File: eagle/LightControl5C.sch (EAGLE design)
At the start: 36 parts, among them IC1 LV3842XF, IC2 PIC12F675, IC3 7805, U1 ULN2003D, X1 Footprint, X10 Footprint, X11 Footprint, X2 Footprint, X3 FLE-103-01, X4 Footprint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

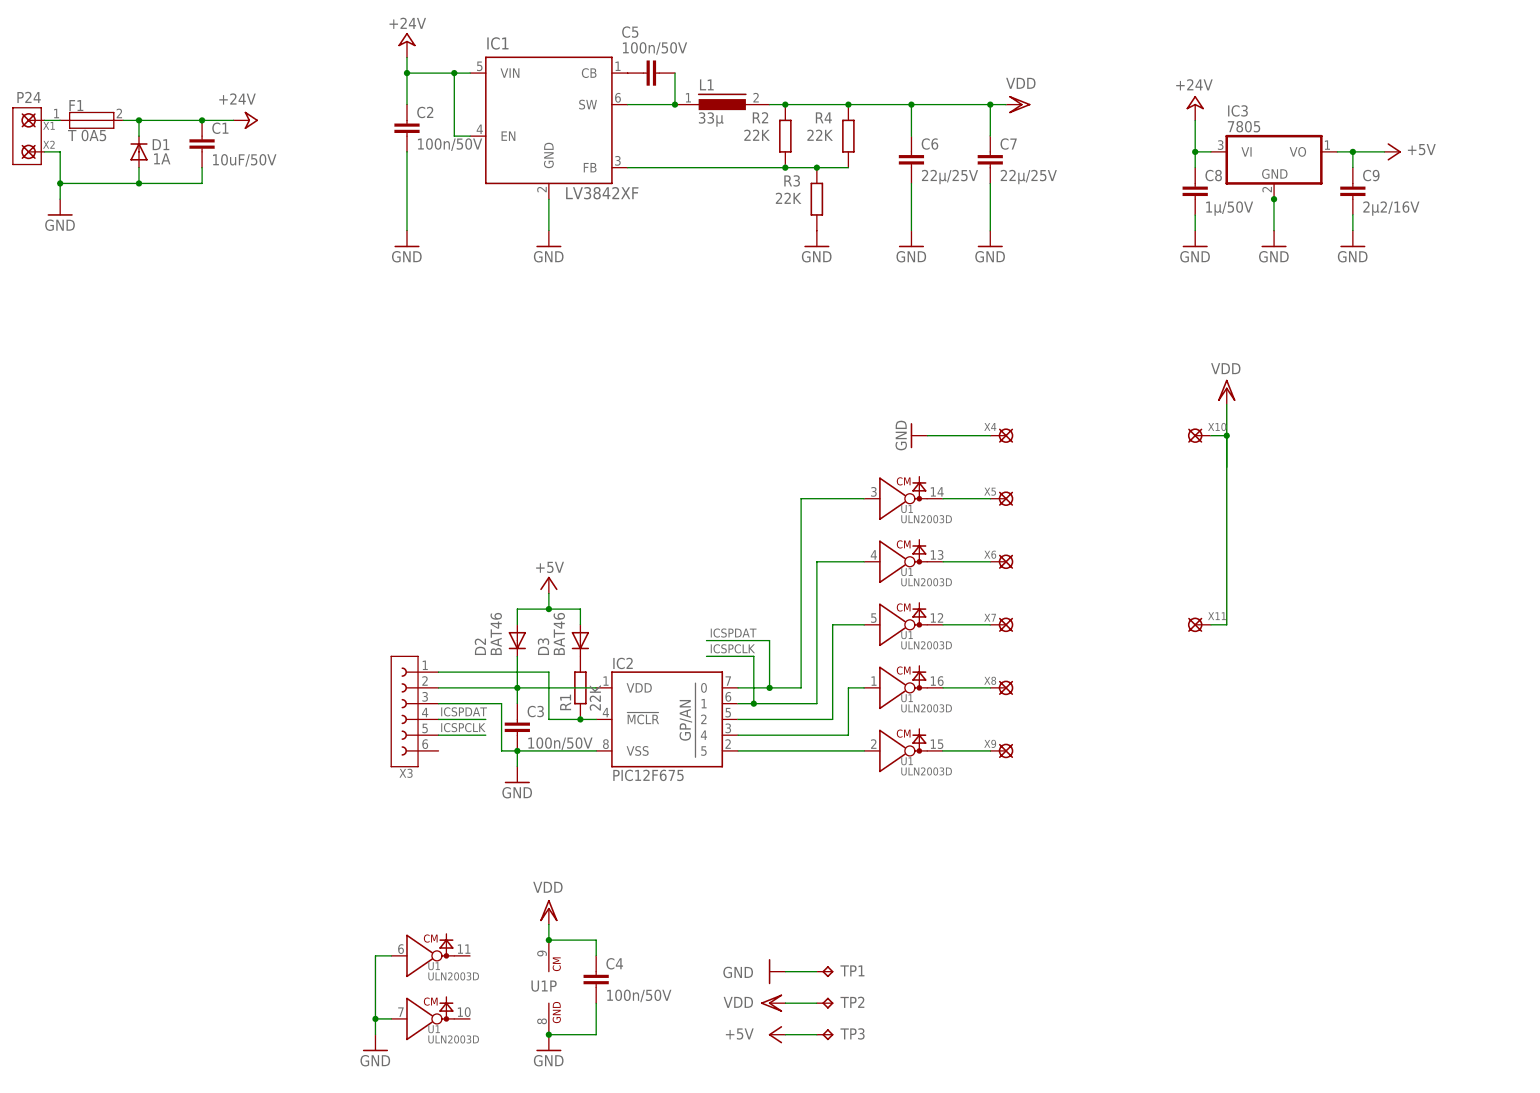
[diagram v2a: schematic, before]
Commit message: [eagle] change inductor
-> increase min. inductor size to allow lower currents
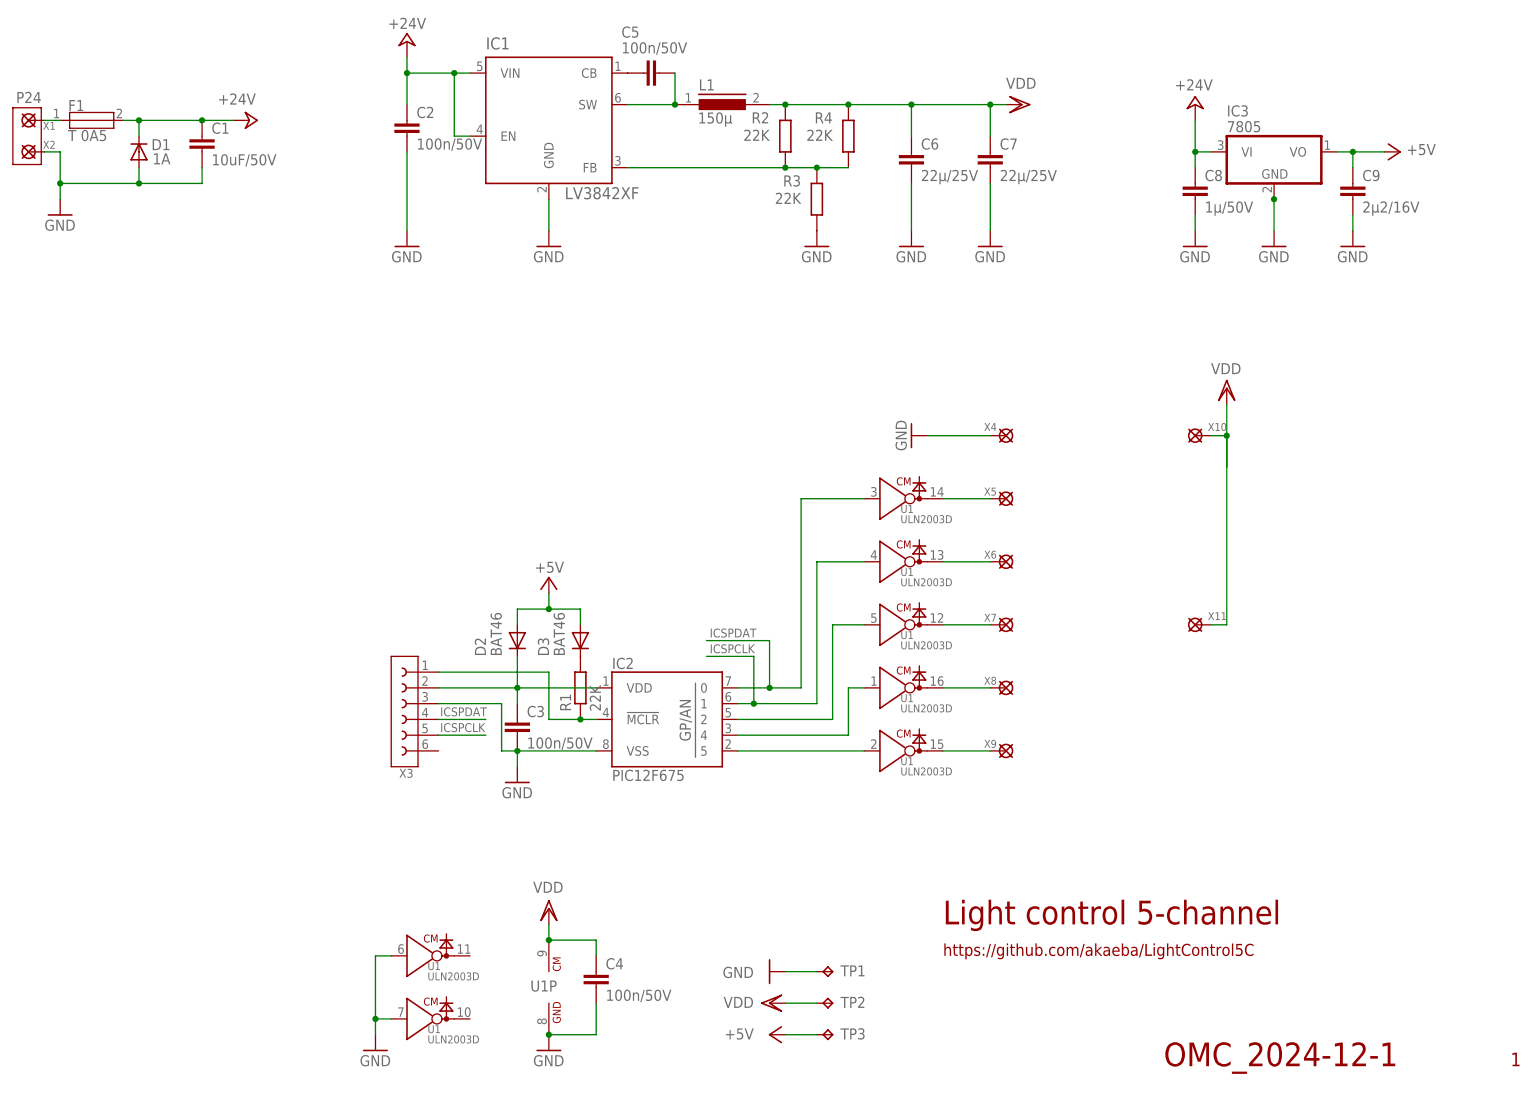
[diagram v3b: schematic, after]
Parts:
- L1: value 33µ -> 150µ; device omcInductor:PISM-33U -> omcInductor:PISM-150U
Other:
- note added: "1.1e6"
- note added: "100u"
- note added: "11V"
- note added: "150u"
- note added: "220u"
- note added: "Light control 5-channel"
- note added: "MIN | Imin=0A1"
- note added: "OMC_2024-12-1"
- note added: "SW"
- note added: "f"
- note added: "https://github.com/akaeba/LightControl5C"
- note removed: "1.1MHz"
- note removed: "22u"
- note removed: "33u"
- note removed: "Remark"
- note removed: "Vmax L1 22u"
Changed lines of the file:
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@@
 <setting verticaltext="up"/>
 </settings>
-<grid distance="0.1" unitdist="inch" unit="inch" style="lines" multiple="1" display="yes" altdistance="0.01" altunitdist="inch" altunit="inch"/>
+<grid distance="0.1" unitdist="inch" unit="inch" style="lines" multiple="1" display="no" altdistance="0.01" altunitdist="inch" altunit="inch"/>
 <layers>
 <layer number="1" name="Top" color="4" fill="1" visible="no" active="no"/>
@@
 <part name="C6" library="omcCapacitor" deviceset="X5R" device="-1210" technology="-22000000P" value="22µ/25V"/>
 <part name="C7" library="omcCapacitor" deviceset="X5R" device="-1210" technology="-22000000P" value="22µ/25V"/>
-<part name="L1" library="omcInductor" deviceset="PISM-" device="" technology="33U" value="33µ"/>
+<part name="L1" library="omcInductor" deviceset="PISM-" device="" technology="150U" value="150µ"/>
 <part name="GND9" library="supply1" deviceset="GND" device=""/>
 <part name="GND11" library="supply1" deviceset="GND" device=""/>
@@
 <text x="151.384" y="155.448" size="1.778" layer="98">R</text>
 <text x="153.162" y="155.194" size="1.016" layer="98">FBT</text>
-<text x="114.808" y="130.048" size="1.778" layer="98">V</text>
-<text x="116.586" y="129.794" size="1.016" layer="98">REF</text>
+<text x="115.316" y="130.048" size="1.778" layer="98">V</text>
+<text x="116.84" y="129.794" size="1.016" layer="98">REF</text>
 <text x="120.142" y="130.048" size="1.778" layer="98">=</text>
 <text x="122.428" y="130.048" size="1.778" layer="98">1.0V</text>
@@
 <text x="175.26" y="48.26" size="1.778" layer="98">Led strips between terminals need proper RV value
 Set VDD level via RFBT according VLED count</text>
-<text x="8.636" y="129.794" size="1.778" layer="98">VDD</text>
-<text x="17.018" y="129.794" size="1.778" layer="98">R</text>
-<text x="18.796" y="129.54" size="1.016" layer="98">FBT</text>
-<wire x1="15.24" y1="132.08" x2="15.24" y2="116.84" width="0.1524" layer="98"/>
-<wire x1="7.62" y1="129.54" x2="66.04" y2="129.54" width="0.1524" layer="98"/>
-<wire x1="25.4" y1="132.08" x2="25.4" y2="116.84" width="0.1524" layer="98"/>
-<wire x1="25.908" y1="132.08" x2="25.908" y2="116.84" width="0.1524" layer="98"/>
-<text x="27.94" y="129.794" size="1.778" layer="98">R2</text>
-<text x="35.56" y="129.794" size="1.778" layer="98">R4</text>
-<text x="43.18" y="129.794" size="1.778" layer="98">L1</text>
+<text x="8.636" y="130.048" size="1.778" layer="98">VDD</text>
+<text x="17.018" y="130.048" size="1.778" layer="98">R</text>
+<text x="18.796" y="129.794" size="1.016" layer="98">FBT</text>
+<wire x1="15.24" y1="132.08" x2="15.24" y2="109.22" width="0.1524" layer="98"/>
+<wire x1="7.62" y1="129.54" x2="60.96" y2="129.54" width="0.1524" layer="98"/>
+<wire x1="25.4" y1="132.08" x2="25.4" y2="109.22" width="0.1524" layer="98"/>
+<wire x1="25.908" y1="132.08" x2="25.908" y2="109.22" width="0.1524" layer="98"/>
+<text x="27.94" y="130.048" size="1.778" layer="98">R2</text>
+<text x="35.56" y="130.048" size="1.778" layer="98">R4</text>
+<text x="45.72" y="130.048" size="1.778" layer="98">L1</text>
 <text x="9.652" y="127.254" size="1.778" layer="98">5V</text>
 <text x="17.018" y="127.254" size="1.778" layer="98">88k</text>
-<text x="43.18" y="127.254" size="1.778" layer="98">22u</text>
+<text x="45.72" y="127.254" size="1.778" layer="98">100u</text>
 <wire x1="175.26" y1="119.38" x2="177.8" y2="119.38" width="0.3048" layer="98"/>
 <wire x1="193.04" y1="110.49" x2="200.66" y2="110.49" width="0.3048" layer="98"/>
@@
 <text x="9.652" y="124.714" size="1.778" layer="98">6V5</text>
 <text x="17.018" y="124.714" size="1.778" layer="98">120k</text>
-<text x="43.18" y="124.714" size="1.778" layer="98">22u</text>
+<text x="45.72" y="124.714" size="1.778" layer="98">150u</text>
 <text x="27.94" y="124.714" size="1.778" layer="98">120k</text>
 <wire x1="37.338" y1="125.73" x2="38.862" y2="125.73" width="0.1524" layer="98"/>
-<text x="9.652" y="119.634" size="1.778" layer="98">16V</text>
-<text x="17.018" y="119.634" size="1.778" layer="98">330k</text>
-<text x="43.18" y="119.634" size="1.778" layer="98">33u</text>
-<text x="35.56" y="119.634" size="1.778" layer="98">330k</text>
-<wire x1="29.718" y1="120.65" x2="31.242" y2="120.65" width="0.1524" layer="98"/>
+<text x="9.652" y="117.094" size="1.778" layer="98">16V</text>
+<text x="17.018" y="117.094" size="1.778" layer="98">330k</text>
+<text x="45.72" y="117.094" size="1.778" layer="98">220u</text>
+<text x="35.56" y="117.094" size="1.778" layer="98">330k</text>
+<wire x1="29.718" y1="118.11" x2="31.242" y2="118.11" width="0.1524" layer="98"/>
 <text x="81.788" y="111.506" size="1.778" layer="98">L</text>
 <text x="83.566" y="111.252" size="1.016" layer="98">MIN</text>
@@
 <text x="90.932" y="109.728" size="1.778" layer="98">0.4</text>
 <text x="94.996" y="110.49" size="1.778" layer="98">.</text>
-<wire x1="105.664" y1="111.76" x2="122.428" y2="111.76" width="0.1524" layer="98"/>
-<text x="112.268" y="112.268" size="1.778" layer="98">V</text>
-<text x="114.046" y="112.014" size="1.016" layer="98">OUT</text>
+<wire x1="105.664" y1="111.76" x2="117.856" y2="111.76" width="0.1524" layer="98"/>
+<text x="109.22" y="112.268" size="1.778" layer="98">V</text>
+<text x="110.998" y="112.014" size="1.016" layer="98">OUT</text>
 <text x="113.284" y="110.49" size="1.778" layer="98">.</text>
 <text x="105.918" y="109.728" size="1.778" layer="98">V</text>
 <text x="107.696" y="109.474" size="1.016" layer="98">IN,MAX</text>
-<text x="114.3" y="109.728" size="1.778" layer="98">1.1MHz</text>
 <text x="104.14" y="111.506" size="1.778" layer="98">.</text>
 <text x="9.652" y="122.174" size="1.778" layer="98">8V2</text>
-<text x="43.18" y="122.174" size="1.778" layer="98">22u</text>
-<wire x1="48.26" y1="132.08" x2="48.26" y2="116.84" width="0.1524" layer="98"/>
-<wire x1="48.768" y1="132.08" x2="48.768" y2="116.84" width="0.1524" layer="98"/>
-<text x="49.784" y="129.794" size="1.778" layer="98">Remark</text>
-<text x="49.784" y="122.174" size="1.778" layer="98">Vmax L1 22u</text>
+<text x="45.72" y="122.174" size="1.778" layer="98">150u</text>
+<wire x1="43.18" y1="132.08" x2="43.18" y2="109.22" width="0.1524" layer="98"/>
+<wire x1="43.688" y1="132.08" x2="43.688" y2="109.22" width="0.1524" layer="98"/>
 <text x="17.018" y="122.174" size="1.778" layer="98">158k4</text>
 <text x="27.94" y="122.174" size="1.778" layer="98">220k</text>
 <text x="35.56" y="122.174" size="1.778" layer="98">560k</text>
+<text x="165.1" y="30.48" size="3.81" layer="94">Light control 5-channel</text>
+<text x="165.1" y="25.4" size="1.9304" layer="94">https://github.com/akaeba/LightControl5C</text>
+<text x="200.66" y="7.62" size="3.81" layer="94">OMC_2024-12-1</text>
+<text x="256.54" y="7.62" size="2.1844" layer="94">1</text>
+<text x="9.652" y="119.634" size="1.778" layer="98">11V</text>
+<text x="17.018" y="119.634" size="1.778" layer="98">220k</text>
+<text x="27.94" y="119.634" size="1.778" layer="98">220k</text>
+<wire x1="37.338" y1="120.65" x2="38.862" y2="120.65" width="0.1524" layer="98"/>
+<text x="116.078" y="127.508" size="1.778" layer="98">f</text>
+<text x="117.094" y="127.254" size="1.016" layer="98">SW</text>
+<text x="120.142" y="127.508" size="1.778" layer="98">=</text>
+<text x="122.428" y="127.508" size="1.778" layer="98">1.1e6</text>
+<text x="114.3" y="109.728" size="1.778" layer="98">f</text>
+<text x="115.316" y="109.474" size="1.016" layer="98">SW</text>
+<text x="48.514" y="130.048" size="1.016" layer="98">MIN | Imin=0A1</text>
+<text x="45.72" y="119.634" size="1.778" layer="98">150u</text>
 </plain>
 <instances>
